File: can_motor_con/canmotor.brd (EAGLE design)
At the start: 50.8 x 50.8 mm, 36 parts

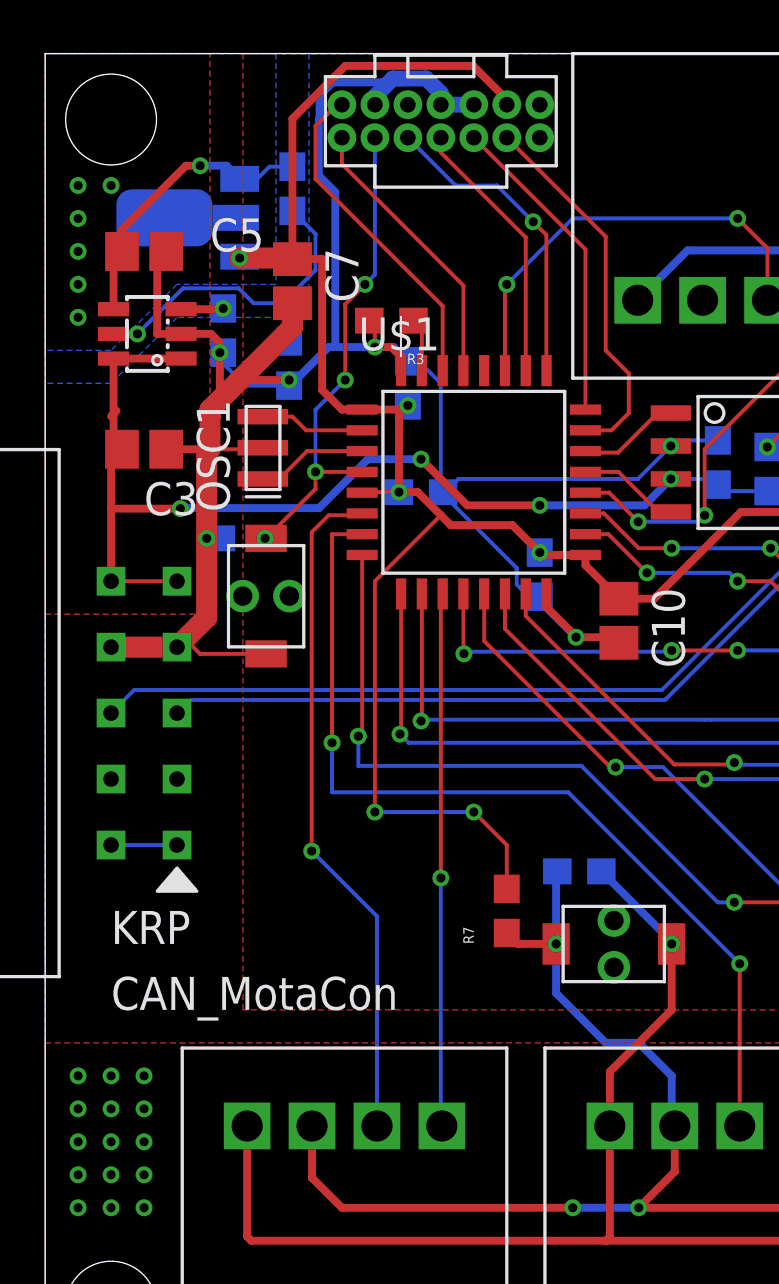
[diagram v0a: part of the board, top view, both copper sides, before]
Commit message: ledをついか
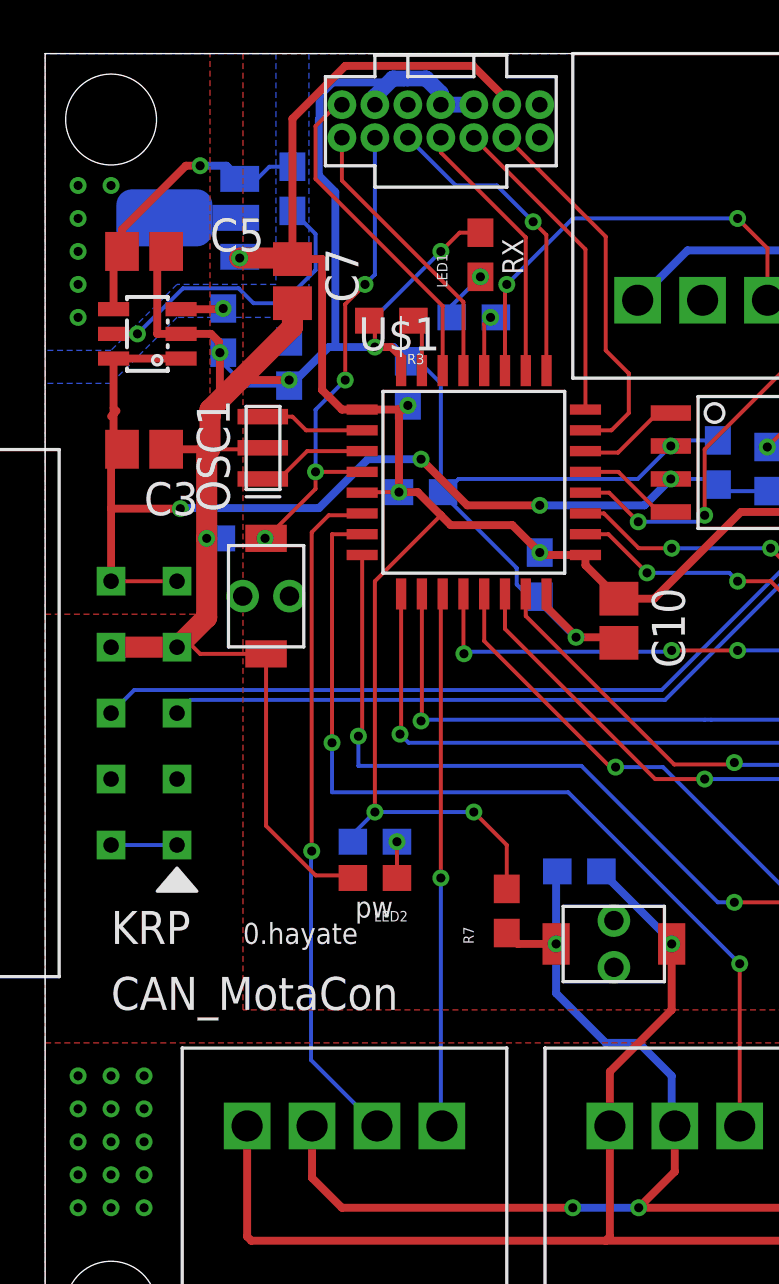
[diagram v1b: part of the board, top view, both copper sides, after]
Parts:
- added LED1, LED2: (no value), user_leds:1608
- added R8, R9: 1k, user_rcl:1608
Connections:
- new net N$11: LED1.A, R8.1
- new net N$12: LED2.A, R9.1
- new net N$14: R8.2, U$1.28
- net GND: now also LED1.K, LED2.K
- net V3.3: now also R9.2
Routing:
- net GND: track 238.5 -> 255.9 mm, vias 52 -> 53
- net N$14: track 0.00 -> 2.36 mm, vias 0 -> 1
- net N$11: track 0.00 -> 2.02 mm, vias 0 -> 1
- net V3.3: track 80.2 -> 81.7 mm
- net N$12: track 0.00 -> 1.40 mm, vias 0 -> 1
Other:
- board text added: "0.hayate"
- board text added: "RX"
- board text added: "pw"
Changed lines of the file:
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@@
 <text x="2.54" y="13.97" size="1.27" layer="21">CAN_MotaCon</text>
 <text x="2.54" y="16.51" size="1.27" layer="21">KRP</text>
+<text x="7.62" y="16.51" size="0.8128" layer="21">0.hayate</text>
+<text x="11.938" y="17.526" size="0.8128" layer="21">pw</text>
+<text x="18.415" y="42.291" size="0.8128" layer="21" rot="R90">RX</text>
 </plain>
 <attributes>
@@
 <attribute name="SPICEPREFIX" value="C" x="37.084" y="33.909" size="1.778" layer="28" rot="MR90" display="off"/>
 </element>
+<element name="LED1" library="user_leds" package="1608" value="" x="16.764" y="43.053" smashed="yes" rot="R90">
+<attribute name="NAME" x="15.494" y="41.783" size="0.4064" layer="25" rot="R90"/>
+<attribute name="VALUE" x="16.002" y="41.783" size="0.4064" layer="27" rot="R90"/>
+</element>
+<element name="LED2" library="user_leds" package="1608" value="" x="12.7" y="19.05" smashed="yes" rot="R180">
+<attribute name="NAME" x="13.97" y="17.78" size="0.4064" layer="25" rot="R180"/>
+<attribute name="VALUE" x="13.97" y="18.288" size="0.4064" layer="27" rot="R180"/>
+</element>
+<element name="R8" library="user_rcl" package="1608" value="1k" x="16.51" y="40.64" smashed="yes" rot="MR180">
+<attribute name="NAME" x="15.24" y="39.37" size="0.4064" layer="26" rot="MR180"/>
+<attribute name="VALUE" x="15.24" y="39.878" size="0.4064" layer="28" rot="MR180"/>
+</element>
+<element name="R9" library="user_rcl" package="1608" value="1k" x="12.7" y="20.447" smashed="yes" rot="MR0">
+<attribute name="NAME" x="13.97" y="21.717" size="0.4064" layer="26" rot="MR0"/>
+<attribute name="VALUE" x="13.97" y="21.209" size="0.4064" layer="28" rot="MR0"/>
+</element>
 </elements>
 <signals>
@@
 <wire x1="12.7" y1="21.59" x2="12.7" y2="30.48" width="0.1524" layer="1"/>
 <wire x1="12.7" y1="30.48" x2="15.24" y2="33.02" width="0.1524" layer="1"/>
+<contactref element="R9" pad="2"/>
+<wire x1="11.85" y1="20.447" x2="11.85" y2="20.74" width="0.1524" layer="16"/>
+<wire x1="11.85" y1="20.74" x2="12.7" y2="21.59" width="0.1524" layer="16"/>
 </signal>
 <signal name="GND">
@@
 <via x="48.26" y="36.83" extent="1-16" drill="0.35"/>
 <via x="49.53" y="36.83" extent="1-16" drill="0.35"/>
+<contactref element="LED1" pad="K"/>
+<contactref element="LED2" pad="K"/>
+<wire x1="16.764" y1="43.903" x2="15.963" y2="43.903" width="0.1524" layer="1"/>
+<wire x1="15.963" y1="43.903" x2="15.24" y2="43.18" width="0.1524" layer="1"/>
+<via x="15.24" y="43.18" extent="1-16" drill="0.35"/>
+<wire x1="15.24" y1="43.18" x2="12.7" y2="40.64" width="0.1524" layer="16"/>
+<wire x1="12.7" y1="40.64" x2="12.7" y2="39.497" width="0.1524" layer="16"/>
+<wire x1="11.85" y1="19.05" x2="11.7506" y2="19.1494" width="0.1524" layer="1"/>
+<wire x1="11.7506" y1="19.1494" x2="10.41729375" y2="19.1494" width="0.1524" layer="1"/>
+<wire x1="10.41729375" y1="19.1494" x2="8.509" y2="21.05769375" width="0.1524" layer="1"/>
+<wire x1="8.509" y1="21.05769375" x2="8.509" y2="27.681" width="0.1524" layer="1"/>
+<wire x1="49.53" y1="44.45" x2="48.26" y2="44.45" width="0" layer="19" extent="1-1"/>
+<wire x1="49.53" y1="43.18" x2="49.53" y2="44.45" width="0" layer="19" extent="1-1"/>
+<wire x1="48.26" y1="43.18" x2="48.26" y2="44.45" width="0" layer="19" extent="1-1"/>
+<wire x1="48.26" y1="41.91" x2="48.26" y2="43.18" width="0" layer="19" extent="1-1"/>
+<wire x1="49.53" y1="41.91" x2="49.53" y2="43.18" width="0" layer="19" extent="1-1"/>
+<wire x1="49.53" y1="40.64" x2="49.53" y2="41.91" width="0" layer="19" extent="1-1"/>
+<wire x1="48.26" y1="40.64" x2="48.26" y2="41.91" width="0" layer="19" extent="1-1"/>
+<wire x1="48.26" y1="39.37" x2="48.26" y2="40.64" width="0" layer="19" extent="1-1"/>
+<wire x1="49.53" y1="39.37" x2="49.53" y2="40.64" width="0" layer="19" extent="1-1"/>
+<wire x1="49.53" y1="38.1" x2="49.53" y2="39.37" width="0" layer="19" extent="1-1"/>
+<wire x1="48.26" y1="38.1" x2="48.26" y2="39.37" width="0" layer="19" extent="1-1"/>
+<wire x1="48.26" y1="36.83" x2="48.26" y2="38.1" width="0" layer="19" extent="1-1"/>
+<wire x1="49.53" y1="36.83" x2="49.53" y2="38.1" width="0" layer="19" extent="1-1"/>
+<wire x1="41.3" y1="30.72" x2="48.26" y2="36.83" width="0" layer="19" extent="1-1"/>
+<wire x1="3.81" y1="8.89" x2="7.78" y2="9.5" width="0" layer="19" extent="1-1"/>
+<wire x1="3.81" y1="10.16" x2="3.81" y2="8.89" width="0" layer="19" extent="1-1"/>
+<wire x1="3.81" y1="11.43" x2="3.81" y2="10.16" width="0" layer="19" extent="1-1"/>
+<wire x1="2.54" y1="11.43" x2="3.81" y2="11.43" width="0" layer="19" extent="1-1"/>
+<wire x1="2.54" y1="10.16" x2="3.81" y2="10.16" width="0" layer="19" extent="1-1"/>
+<wire x1="1.27" y1="11.43" x2="2.54" y2="11.43" width="0" layer="19" extent="1-1"/>
+<wire x1="1.27" y1="10.16" x2="2.54" y2="10.16" width="0" layer="19" extent="1-1"/>
+<wire x1="2.54" y1="8.89" x2="3.81" y2="8.89" width="0" layer="19" extent="1-1"/>
+<wire x1="2.54" y1="7.62" x2="2.54" y2="8.89" width="0" layer="19" extent="1-1"/>
+<wire x1="3.81" y1="7.62" x2="3.81" y2="8.89" width="0" layer="19" extent="1-1"/>
+<wire x1="1.27" y1="8.89" x2="1.27" y2="10.16" width="0" layer="19" extent="1-1"/>
+<wire x1="1.27" y1="7.62" x2="2.54" y2="7.62" width="0" layer="19" extent="1-1"/>
+<wire x1="3.81" y1="6.35" x2="3.81" y2="7.62" width="0" layer="19" extent="1-1"/>
+<wire x1="2.54" y1="6.35" x2="2.54" y2="7.62" width="0" layer="19" extent="1-1"/>
+<wire x1="1.27" y1="6.35" x2="1.27" y2="7.62" width="0" layer="19" extent="1-1"/>
+<wire x1="46.99" y1="11.43" x2="41.3" y2="16.67" width="0" layer="19" extent="1-1"/>
+<wire x1="48.26" y1="11.43" x2="46.99" y2="11.43" width="0" layer="19" extent="1-1"/>
+<wire x1="48.26" y1="10.16" x2="48.26" y2="11.43" width="0" layer="19" extent="1-1"/>
+<wire x1="49.53" y1="10.16" x2="48.26" y2="10.16" width="0" layer="19" extent="1-1"/>
+<wire x1="49.53" y1="11.43" x2="48.26" y2="11.43" width="0" layer="19" extent="1-1"/>
+<wire x1="48.26" y1="8.89" x2="48.26" y2="10.16" width="0" layer="19" extent="1-1"/>
+<wire x1="48.26" y1="7.62" x2="48.26" y2="8.89" width="0" layer="19" extent="1-1"/>
+<wire x1="49.53" y1="7.62" x2="48.26" y2="7.62" width="0" layer="19" extent="1-1"/>
+<wire x1="49.53" y1="8.89" x2="49.53" y2="10.16" width="0" layer="19" extent="1-1"/>
+<wire x1="46.99" y1="10.16" x2="46.99" y2="11.43" width="0" layer="19" extent="1-1"/>
+<wire x1="48.26" y1="6.35" x2="48.26" y2="7.62" width="0" layer="19" extent="1-1"/>
+<wire x1="49.53" y1="6.35" x2="49.53" y2="7.62" width="0" layer="19" extent="1-1"/>
+<wire x1="46.99" y1="7.62" x2="48.26" y2="7.62" width="0" layer="19" extent="1-1"/>
+<wire x1="46.99" y1="8.89" x2="48.26" y2="8.89" width="0" layer="19" extent="1-1"/>
+<wire x1="46.99" y1="6.35" x2="48.26" y2="6.35" width="0" layer="19" extent="1-1"/>
+<wire x1="22.098" y1="28.106" x2="21.424" y2="19.304" width="0" layer="19" extent="1-16"/>
+<wire x1="6.858" y1="39.282" x2="6.731" y2="39.282" width="0" layer="19" extent="16-16"/>
 </signal>
 <signal name="VCC">
@@
 <contactref element="U$6" pad="14"/>
 <contactref element="U$1" pad="29"/>
-<wire x1="16.11" y1="41.865" x2="11.43" y2="46.545" width="0.1524" layer="1"/>
-<wire x1="11.43" y1="47.561" x2="11.43" y2="46.545" width="0.1524" layer="1"/>
-<wire x1="16.11" y1="41.865" x2="16.11" y2="38.59" width="0.1524" layer="1"/>
+<wire x1="16.11" y1="41.23" x2="11.43" y2="45.91" width="0.1524" layer="1"/>
+<wire x1="11.43" y1="47.561" x2="11.43" y2="45.91" width="0.1524" layer="1"/>
+<wire x1="16.11" y1="41.23" x2="16.11" y2="38.59" width="0.1524" layer="1"/>
 </signal>
 <signal name="TIM2_CH1">
@@
 <wire x1="10.922" y1="33.02" x2="10.2666" y2="32.3646" width="0.1524" layer="1"/>
 <via x="10.2666" y="20.0864" extent="1-16" drill="0.35"/>
-<wire x1="10.2666" y1="20.0864" x2="12.78" y2="17.573" width="0.1524" layer="16"/>
-<wire x1="12.78" y1="17.573" x2="12.78" y2="9.5" width="0.1524" layer="16"/>
+<wire x1="10.2666" y1="20.0864" x2="10.24" y2="20.0598" width="0.1524" layer="16"/>
+<wire x1="10.24" y1="20.0598" x2="10.24" y2="12.04" width="0.1524" layer="16"/>
+<wire x1="10.24" y1="12.04" x2="12.78" y2="9.5" width="0.1524" layer="16"/>
 <wire x1="10.2666" y1="32.3646" x2="10.2666" y2="20.0864" width="0.1524" layer="1"/>
 </signal>
@@
 <wire x1="29.86" y1="22.86" x2="43.22" y2="9.5" width="0.1524" layer="16"/>
 </signal>
+<signal name="N$11">
+<contactref element="LED1" pad="A"/>
+<contactref element="R8" pad="1"/>
+<wire x1="15.66" y1="40.64" x2="15.66" y2="41.099" width="0.1524" layer="16"/>
+<wire x1="15.66" y1="41.099" x2="16.764" y2="42.203" width="0.1524" layer="16"/>
+<via x="16.764" y="42.203" extent="1-16" drill="0.35"/>
+</signal>
+<signal name="N$12">
+<contactref element="LED2" pad="A"/>
+<contactref element="R9" pad="1"/>
+<wire x1="13.55" y1="19.05" x2="13.55" y2="20.447" width="0.1524" layer="1"/>
+<via x="13.55" y="20.447" extent="1-16" drill="0.35"/>
+</signal>
+<signal name="N$14">
+<contactref element="R8" pad="2"/>
+<contactref element="U$1" pad="28"/>
+<wire x1="16.91" y1="38.59" x2="16.91" y2="40.396" width="0.1524" layer="1"/>
+<wire x1="16.91" y1="40.396" x2="17.154" y2="40.64" width="0.1524" layer="1"/>
+<via x="17.154" y="40.64" extent="1-16" drill="0.35"/>
+<wire x1="17.154" y1="40.64" x2="17.36" y2="40.64" width="0.1524" layer="16"/>
+</signal>
 </signals>

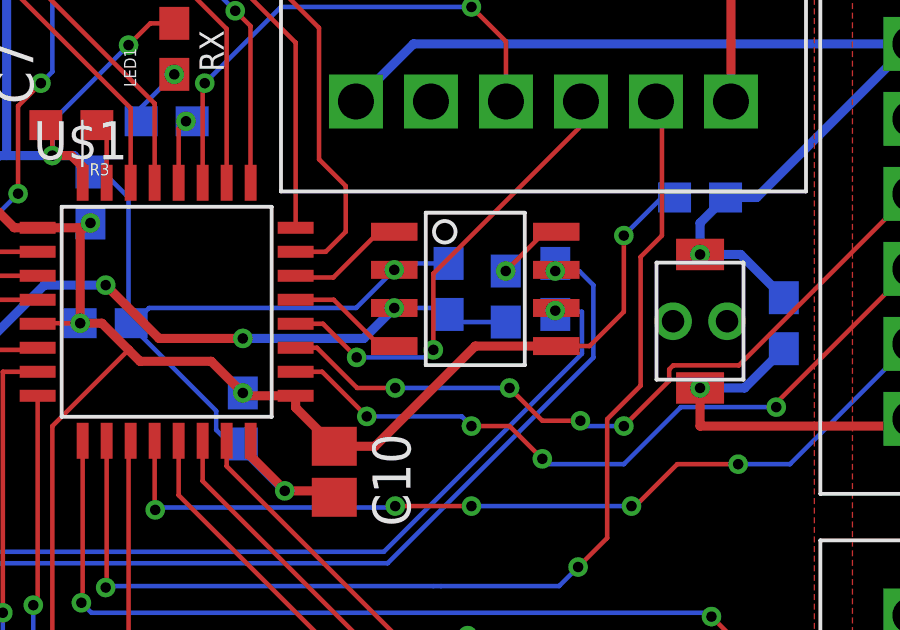
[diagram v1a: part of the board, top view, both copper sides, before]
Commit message: mcp2562スタンバイピンプルダウン
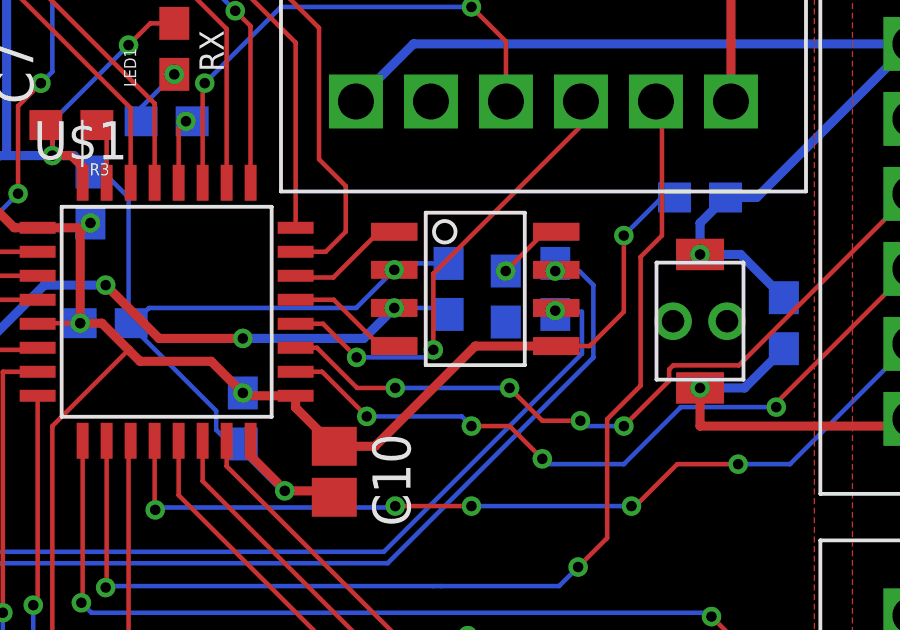
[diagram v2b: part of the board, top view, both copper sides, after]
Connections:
- net GND: now also R4.2
- net VCC: no longer R4.2
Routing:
- net VCC: track 42.7 -> 40.7 mm
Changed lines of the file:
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@@
 <wire x1="10.41729375" y1="19.1494" x2="8.509" y2="21.05769375" width="0.1524" layer="1"/>
 <wire x1="8.509" y1="21.05769375" x2="8.509" y2="27.681" width="0.1524" layer="1"/>
-<wire x1="49.53" y1="44.45" x2="48.26" y2="44.45" width="0" layer="19" extent="1-1"/>
-<wire x1="49.53" y1="43.18" x2="49.53" y2="44.45" width="0" layer="19" extent="1-1"/>
-<wire x1="48.26" y1="43.18" x2="48.26" y2="44.45" width="0" layer="19" extent="1-1"/>
-<wire x1="48.26" y1="41.91" x2="48.26" y2="43.18" width="0" layer="19" extent="1-1"/>
-<wire x1="49.53" y1="41.91" x2="49.53" y2="43.18" width="0" layer="19" extent="1-1"/>
-<wire x1="49.53" y1="40.64" x2="49.53" y2="41.91" width="0" layer="19" extent="1-1"/>
-<wire x1="48.26" y1="40.64" x2="48.26" y2="41.91" width="0" layer="19" extent="1-1"/>
-<wire x1="48.26" y1="39.37" x2="48.26" y2="40.64" width="0" layer="19" extent="1-1"/>
-<wire x1="49.53" y1="39.37" x2="49.53" y2="40.64" width="0" layer="19" extent="1-1"/>
-<wire x1="49.53" y1="38.1" x2="49.53" y2="39.37" width="0" layer="19" extent="1-1"/>
-<wire x1="48.26" y1="38.1" x2="48.26" y2="39.37" width="0" layer="19" extent="1-1"/>
-<wire x1="48.26" y1="36.83" x2="48.26" y2="38.1" width="0" layer="19" extent="1-1"/>
-<wire x1="49.53" y1="36.83" x2="49.53" y2="38.1" width="0" layer="19" extent="1-1"/>
-<wire x1="41.3" y1="30.72" x2="48.26" y2="36.83" width="0" layer="19" extent="1-1"/>
-<wire x1="3.81" y1="8.89" x2="7.78" y2="9.5" width="0" layer="19" extent="1-1"/>
-<wire x1="3.81" y1="10.16" x2="3.81" y2="8.89" width="0" layer="19" extent="1-1"/>
-<wire x1="3.81" y1="11.43" x2="3.81" y2="10.16" width="0" layer="19" extent="1-1"/>
-<wire x1="2.54" y1="11.43" x2="3.81" y2="11.43" width="0" layer="19" extent="1-1"/>
-<wire x1="2.54" y1="10.16" x2="3.81" y2="10.16" width="0" layer="19" extent="1-1"/>
-<wire x1="1.27" y1="11.43" x2="2.54" y2="11.43" width="0" layer="19" extent="1-1"/>
-<wire x1="1.27" y1="10.16" x2="2.54" y2="10.16" width="0" layer="19" extent="1-1"/>
-<wire x1="2.54" y1="8.89" x2="3.81" y2="8.89" width="0" layer="19" extent="1-1"/>
-<wire x1="2.54" y1="7.62" x2="2.54" y2="8.89" width="0" layer="19" extent="1-1"/>
-<wire x1="3.81" y1="7.62" x2="3.81" y2="8.89" width="0" layer="19" extent="1-1"/>
-<wire x1="1.27" y1="8.89" x2="1.27" y2="10.16" width="0" layer="19" extent="1-1"/>
-<wire x1="1.27" y1="7.62" x2="2.54" y2="7.62" width="0" layer="19" extent="1-1"/>
-<wire x1="3.81" y1="6.35" x2="3.81" y2="7.62" width="0" layer="19" extent="1-1"/>
-<wire x1="2.54" y1="6.35" x2="2.54" y2="7.62" width="0" layer="19" extent="1-1"/>
-<wire x1="1.27" y1="6.35" x2="1.27" y2="7.62" width="0" layer="19" extent="1-1"/>
-<wire x1="46.99" y1="11.43" x2="41.3" y2="16.67" width="0" layer="19" extent="1-1"/>
-<wire x1="48.26" y1="11.43" x2="46.99" y2="11.43" width="0" layer="19" extent="1-1"/>
-<wire x1="48.26" y1="10.16" x2="48.26" y2="11.43" width="0" layer="19" extent="1-1"/>
-<wire x1="49.53" y1="10.16" x2="48.26" y2="10.16" width="0" layer="19" extent="1-1"/>
-<wire x1="49.53" y1="11.43" x2="48.26" y2="11.43" width="0" layer="19" extent="1-1"/>
-<wire x1="48.26" y1="8.89" x2="48.26" y2="10.16" width="0" layer="19" extent="1-1"/>
-<wire x1="48.26" y1="7.62" x2="48.26" y2="8.89" width="0" layer="19" extent="1-1"/>
-<wire x1="49.53" y1="7.62" x2="48.26" y2="7.62" width="0" layer="19" extent="1-1"/>
-<wire x1="49.53" y1="8.89" x2="49.53" y2="10.16" width="0" layer="19" extent="1-1"/>
-<wire x1="46.99" y1="10.16" x2="46.99" y2="11.43" width="0" layer="19" extent="1-1"/>
-<wire x1="48.26" y1="6.35" x2="48.26" y2="7.62" width="0" layer="19" extent="1-1"/>
-<wire x1="49.53" y1="6.35" x2="49.53" y2="7.62" width="0" layer="19" extent="1-1"/>
-<wire x1="46.99" y1="7.62" x2="48.26" y2="7.62" width="0" layer="19" extent="1-1"/>
-<wire x1="46.99" y1="8.89" x2="48.26" y2="8.89" width="0" layer="19" extent="1-1"/>
-<wire x1="46.99" y1="6.35" x2="48.26" y2="6.35" width="0" layer="19" extent="1-1"/>
-<wire x1="22.098" y1="28.106" x2="21.424" y2="19.304" width="0" layer="19" extent="1-16"/>
-<wire x1="6.858" y1="39.282" x2="6.731" y2="39.282" width="0" layer="19" extent="16-16"/>
+<contactref element="R4" pad="2"/>
 </signal>
 <signal name="VCC">
@@
 <contactref element="BOX10P-L2" pad="P$10"/>
 <contactref element="U$5" pad="P$3"/>
-<contactref element="R4" pad="2"/>
 <wire x1="2.637" y1="39.055" x2="5.237" y2="39.055" width="0.3048" layer="1"/>
 <wire x1="2.96" y1="35.56" x2="2.54" y2="35.98" width="0.1524" layer="1"/>
 <wire x1="2.75" y1="37.04" x2="2.637" y2="37.153" width="0.1524" layer="1"/>
-<wire x1="25.908" y1="34.202" x2="26.162" y2="33.948" width="0.1524" layer="16"/>
-<wire x1="27.813" y1="33.948" x2="26.162" y2="33.948" width="0.1524" layer="16"/>
 <via x="24.097" y="34.417" extent="1-16" drill="0.35"/>
 <wire x1="24.097" y1="34.417" x2="23.081" y2="33.401" width="0.3048" layer="16"/>
@@
 </polygon>
 <contactref element="C11" pad="2"/>
-<wire x1="24.097" y1="34.417" x2="25.693" y2="34.417" width="0.1524" layer="16"/>
-<wire x1="25.693" y1="34.417" x2="25.908" y2="34.202" width="0.1524" layer="16"/>
+<wire x1="25.693" y1="34.417" x2="24.097" y2="34.417" width="0.1524" layer="16"/>
 <wire x1="5.207" y1="33.274" x2="2.54" y2="33.274" width="0.3048" layer="1"/>
 <via x="5.207" y="33.274" extent="1-16" drill="0.35"/>
@@
 <wire x1="10.54886875" y1="33.2958" x2="5.2288" y2="33.2958" width="0.3048" layer="16"/>
 <wire x1="5.207" y1="33.274" x2="5.2288" y2="33.2958" width="0.3048" layer="16"/>
+<wire x1="25.908" y1="34.202" x2="25.693" y2="34.417" width="0.1524" layer="16"/>
 </signal>
 <signal name="N$3">
